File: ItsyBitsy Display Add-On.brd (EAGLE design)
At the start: 35.6 x 17.8 mm, 15 parts, among them IC1 APX803, SW1 SPST_TACT-KMR2

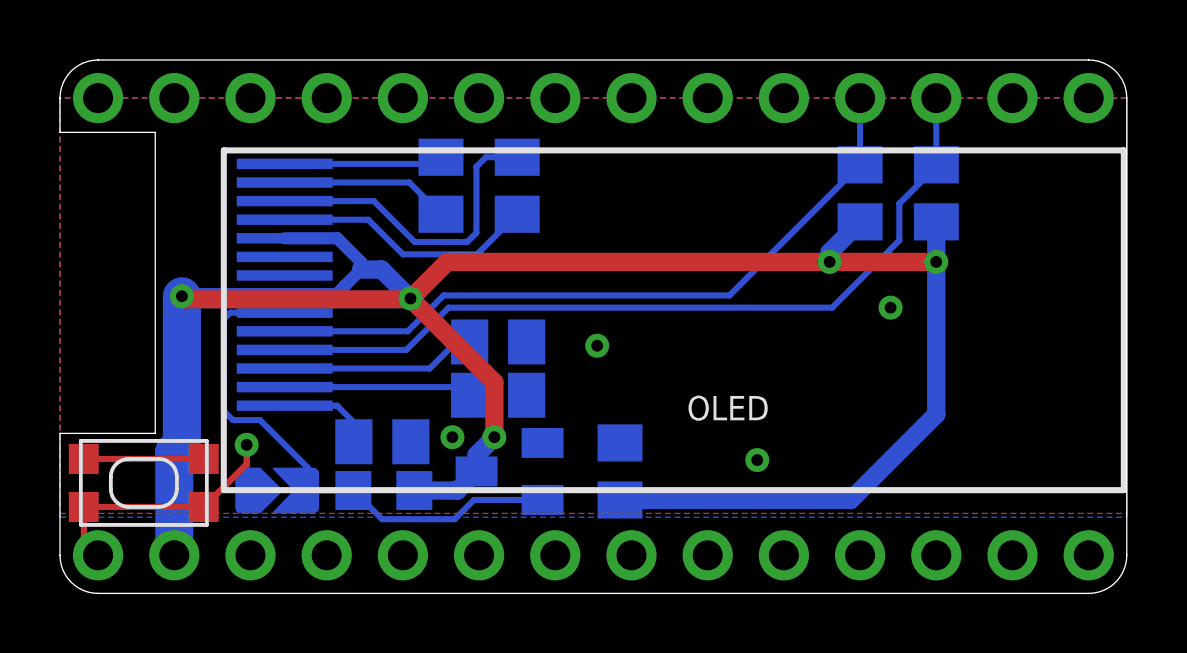
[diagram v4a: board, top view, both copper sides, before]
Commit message: Moved C3, flipped jumper
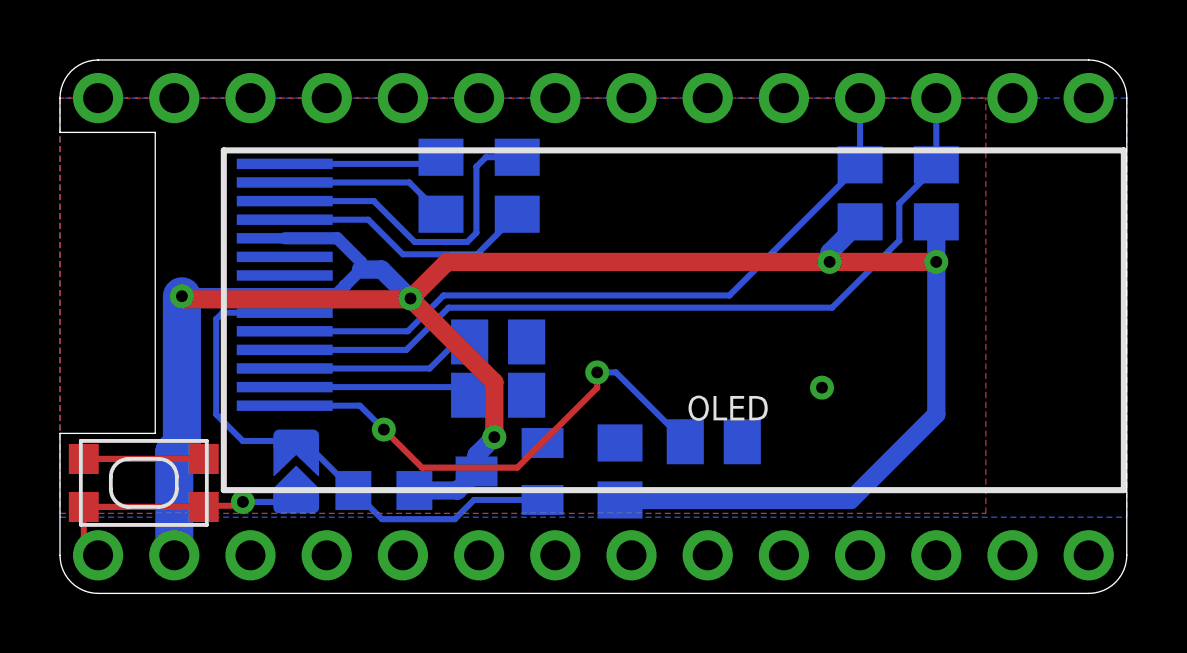
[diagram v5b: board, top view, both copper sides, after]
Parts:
- moved C3 11.0 mm to (21.8, 5.05)
- moved SJ1 0.90 mm to (7.87, 4.06), turned to 90 degrees
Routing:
- net VCC: track 4.28 -> 18.5 mm, vias 0 -> 2
- net !RESET: track 10.00 -> 8.96 mm
- net GND: vias 2 -> 1
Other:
- board text added: "+OLED_RST"
- board text removed: "PAD +Board RST to switch"
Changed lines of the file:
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@@
 <drawing>
 <settings>
-<setting alwaysvectorfont="no"/>
+<setting alwaysvectorfont="yes"/>
 <setting keepoldvectorfont="yes"/>
 <setting verticaltext="up"/>
@@
 <wire x1="3.175" y1="15.367" x2="3.175" y2="5.334" width="0" layer="20"/>
 <wire x1="3.175" y1="5.334" x2="0" y2="5.334" width="0" layer="20"/>
-<text x="25.908" y="9.017" size="1.016" layer="22" font="vector" ratio="12" distance="30" rot="MR0" align="center">128x32 Monochrome
+<text x="26.416" y="9.017" size="1.016" layer="22" font="vector" ratio="12" distance="30" rot="MR0" align="center">128x32 Monochrome
 OLED BitsyWing</text>
-<text x="25.908" y="5.334" size="1.4224" layer="22" font="vector" ratio="14" rot="MR0" align="center">HEXTHAT</text>
-<text x="16.383" y="11.049" size="0.8128" layer="22" font="vector" ratio="13" distance="20" rot="MR0" align="center">PAD +Board RST
-to switch</text>
+<text x="28.829" y="3.683" size="1.4224" layer="22" font="vector" ratio="14" rot="MR0" align="center">HEXTHAT</text>
+<text x="4.826" y="5.588" size="0.8128" layer="22" font="vector" ratio="13" distance="20" rot="MR270" align="center">+OLED_RST</text>
 </plain>
 <attributes>
@@
 </element>
 <element name="C1" library="microbuilder" package="0805-NO" value="10uF" x="18.669" y="4.064" smashed="yes" rot="MR270">
-<attribute name="NAME" x="20.447" y="4.572" size="0.8128" layer="26" ratio="18" rot="MR270"/>
+<attribute name="NAME" x="20.447" y="3.937" size="0.8128" layer="26" ratio="18" rot="MR270"/>
 <attribute name="VALUE" x="19.431" y="2.032" size="0.4064" layer="28" ratio="10" rot="MR270"/>
 </element>
-<element name="C3" library="microbuilder" package="0805-NO" value="10uF" x="10.7442" y="5.0546" smashed="yes" rot="MR0">
-<attribute name="NAME" x="11.3792" y="5.8166" size="0.8128" layer="26" ratio="18" rot="MR0"/>
-<attribute name="VALUE" x="8.7122" y="4.2926" size="0.4064" layer="28" ratio="10" rot="MR0"/>
+<element name="C3" library="microbuilder" package="0805-NO" value="10uF" x="21.7932" y="5.0546" smashed="yes" rot="MR0">
+<attribute name="NAME" x="22.5552" y="6.0706" size="0.8128" layer="26" ratio="18" rot="MR0"/>
+<attribute name="VALUE" x="19.7612" y="4.2926" size="0.4064" layer="28" ratio="10" rot="MR0"/>
 </element>
 <element name="C2" library="microbuilder" package="0805-NO" value="10uF" x="14.605" y="6.604" smashed="yes" rot="MR0">
@@
 </element>
 <element name="R2" library="microbuilder" package="_0805MP" value="10K" x="10.795" y="3.429" smashed="yes" rot="MR180">
-<attribute name="NAME" x="12.7635" y="2.9845" size="0.8128" layer="26" ratio="18" rot="MR180"/>
+<attribute name="NAME" x="10.2235" y="5.0165" size="0.8128" layer="26" ratio="18" rot="MR180"/>
 <attribute name="VALUE" x="9.2075" y="4.699" size="0.4064" layer="28" ratio="10" rot="MR180"/>
 </element>
-<element name="SJ1" library="microbuilder" package="SOLDERJUMPER_ARROW_NOPASTE" value="" x="7.239" y="3.429" smashed="yes" rot="MR180">
-<attribute name="BOM" value="EXCLUDE" x="3.429" y="7.366" size="1.778" layer="28" rot="MR180" display="off"/>
-<attribute name="VALUE" x="5.588" y="5.08" size="0.4064" layer="28" ratio="10" rot="MR180"/>
+<element name="SJ1" library="microbuilder" package="SOLDERJUMPER_ARROW_NOPASTE" value="" x="7.874" y="4.064" smashed="yes" rot="MR90">
+<attribute name="BOM" value="EXCLUDE" x="3.937" y="0.254" size="1.778" layer="28" rot="MR90" display="off"/>
+<attribute name="VALUE" x="6.223" y="2.413" size="0.4064" layer="28" ratio="10" rot="MR90"/>
 </element>
 </elements>
@@
 <vertex x="0" y="16.51"/>
 <vertex x="0" y="2.667"/>
-<vertex x="35.56" y="2.667"/>
-<vertex x="35.56" y="16.51"/>
+<vertex x="30.861" y="2.667"/>
+<vertex x="30.861" y="16.51"/>
 </polygon>
 <polygon width="0.254" layer="16">
@@
 <contactref element="C1" pad="1"/>
 <contactref element="IC1" pad="1"/>
-<via x="13.081" y="5.207" extent="1-16" drill="0.3937"/>
 <wire x1="0.794" y1="4.483" x2="4.794" y2="4.483" width="0.2032" layer="1"/>
-<via x="27.686" y="9.525" extent="1-16" drill="0.3937"/>
+<via x="25.4" y="6.858" extent="1-16" drill="0.3937"/>
 </signal>
 <signal name="MOSI">
@@
 <contactref element="JP2" pad="14"/>
 <contactref element="SJ1" pad="1"/>
-<wire x1="6.223" y1="3.429" x2="6.223" y2="4.953" width="0.2032" layer="16"/>
+<wire x1="7.874" y1="3.048" x2="6.096" y2="3.048" width="0.2032" layer="16"/>
 <wire x1="1.27" y1="1.27" x2="0.794" y2="1.746" width="0.2032" layer="1"/>
 <wire x1="0.794" y1="1.746" x2="0.794" y2="2.883" width="0.2032" layer="1"/>
 <wire x1="0.794" y1="2.883" x2="4.794" y2="2.883" width="0.2032" layer="1"/>
-<wire x1="4.794" y1="2.883" x2="6.223" y2="4.312" width="0.2032" layer="1"/>
-<wire x1="6.223" y1="4.312" x2="6.223" y2="4.953" width="0.2032" layer="1"/>
-<via x="6.223" y="4.953" extent="1-16" drill="0.3937"/>
+<wire x1="4.794" y1="2.883" x2="4.832" y2="2.921" width="0.2032" layer="1"/>
+<wire x1="5.969" y1="2.921" x2="6.096" y2="3.048" width="0.2032" layer="1"/>
+<wire x1="5.969" y1="2.921" x2="4.832" y2="2.921" width="0.2032" layer="1"/>
+<via x="6.096" y="3.048" extent="1-16" drill="0.3937"/>
 </signal>
 <signal name="D2">
@@
 <contactref element="C3" pad="2"/>
 <wire x1="7.491" y1="6.257" x2="8.5918" y2="6.257" width="0.2032" layer="16"/>
-<wire x1="9.7942" y1="5.0546" x2="9.7942" y2="5.6998" width="0.2032" layer="16"/>
-<wire x1="9.237" y1="6.257" x2="7.491" y2="6.257" width="0.2032" layer="16"/>
-<wire x1="9.7942" y1="5.6998" x2="9.237" y2="6.257" width="0.2032" layer="16"/>
+<wire x1="20.8432" y1="5.0546" x2="20.8432" y2="5.6998" width="0.2032" layer="16"/>
+<wire x1="7.491" y1="6.257" x2="9.999" y2="6.257" width="0.2032" layer="16"/>
+<wire x1="9.999" y1="6.257" x2="10.795" y2="5.461" width="0.2032" layer="16"/>
+<via x="10.795" y="5.461" extent="1-16" drill="0.3937"/>
+<via x="17.907" y="7.366" extent="1-16" drill="0.3937"/>
+<wire x1="20.8432" y1="5.0546" x2="18.5318" y2="7.366" width="0.2032" layer="16"/>
+<wire x1="18.5318" y1="7.366" x2="17.907" y2="7.366" width="0.2032" layer="16"/>
+<wire x1="17.907" y1="7.366" x2="17.907" y2="6.858" width="0.2032" layer="1"/>
+<wire x1="17.907" y1="6.858" x2="15.24" y2="4.191" width="0.2032" layer="1"/>
+<wire x1="12.065" y1="4.191" x2="10.795" y2="5.461" width="0.2032" layer="1"/>
+<wire x1="15.24" y1="4.191" x2="12.065" y2="4.191" width="0.2032" layer="1"/>
 </signal>
 <signal name="3.3V">
@@
 <contactref element="R2" pad="1"/>
 <contactref element="SJ1" pad="2"/>
-<wire x1="7.491" y1="9.357" x2="5.674" y2="9.357" width="0.2032" layer="16"/>
-<wire x1="5.674" y1="9.357" x2="5.461" y2="9.144" width="0.2032" layer="16"/>
-<wire x1="5.76475" y1="5.7772" x2="6.6688" y2="5.7772" width="0.2032" layer="16"/>
-<wire x1="5.461" y1="9.144" x2="5.461" y2="6.08095" width="0.2032" layer="16"/>
-<wire x1="5.461" y1="6.08095" x2="5.76475" y2="5.7772" width="0.2032" layer="16"/>
-<wire x1="8.255" y1="4.191" x2="8.255" y2="3.429" width="0.2032" layer="16"/>
-<wire x1="6.6688" y1="5.7772" x2="8.255" y2="4.191" width="0.2032" layer="16"/>
-<wire x1="9.779" y1="3.429" x2="8.255" y2="3.429" width="0.2032" layer="16"/>
 <wire x1="16.086" y1="3.114" x2="13.79810625" y2="3.114" width="0.2032" layer="16"/>
 <wire x1="13.79810625" y1="3.114" x2="13.15830625" y2="2.4742" width="0.2032" layer="16"/>
 <wire x1="13.15830625" y1="2.4742" x2="10.7338" y2="2.4742" width="0.2032" layer="16"/>
 <wire x1="10.7338" y1="2.4742" x2="9.779" y2="3.429" width="0.2032" layer="16"/>
-</signal>
-<signal name="N$8">
-<via x="17.907" y="8.255" extent="1-16" drill="0.3937"/>
-</signal>
-<signal name="N$9">
-<via x="23.241" y="4.445" extent="1-16" drill="0.3937"/>
+<wire x1="7.491" y1="9.357" x2="5.42" y2="9.357" width="0.2032" layer="16"/>
+<wire x1="5.42" y1="9.357" x2="5.207" y2="9.144" width="0.2032" layer="16"/>
+<wire x1="5.207" y1="9.144" x2="5.207" y2="5.969" width="0.2032" layer="16"/>
+<wire x1="6.096" y1="5.08" x2="7.874" y2="5.08" width="0.2032" layer="16"/>
+<wire x1="5.207" y1="5.969" x2="6.096" y2="5.08" width="0.2032" layer="16"/>
+<wire x1="9.779" y1="3.429" x2="8.128" y2="5.08" width="0.2032" layer="16"/>
+<wire x1="8.128" y1="5.08" x2="7.874" y2="5.08" width="0.2032" layer="16"/>
 </signal>
 </signals>
